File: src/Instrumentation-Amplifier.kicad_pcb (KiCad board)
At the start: 2 copper layers, 24.1 x 34.3 mm, 10 parts, among them J1 PPTC041LFBN-RC, J2 PPTC041LFBN-RC, U1 LM7812_SMD, U2 AD623ARZ-R7

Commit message: Cleaned up file structure
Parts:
- D1: value LTST-C150GKT -> LED_LTST-C150GKT_LTO
- U2: value AD623ARZ-R7 -> R_8_ADI

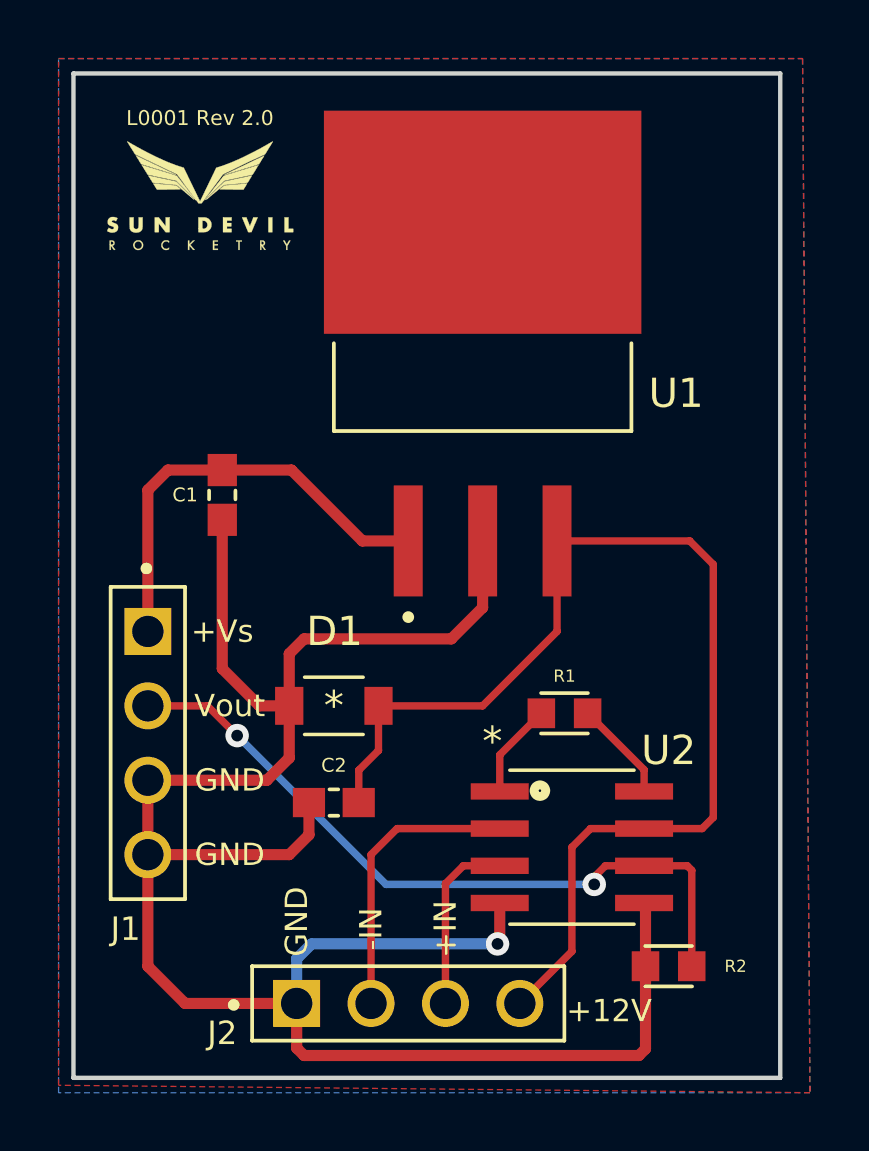
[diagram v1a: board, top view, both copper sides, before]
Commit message: Updated PCB with new connectors
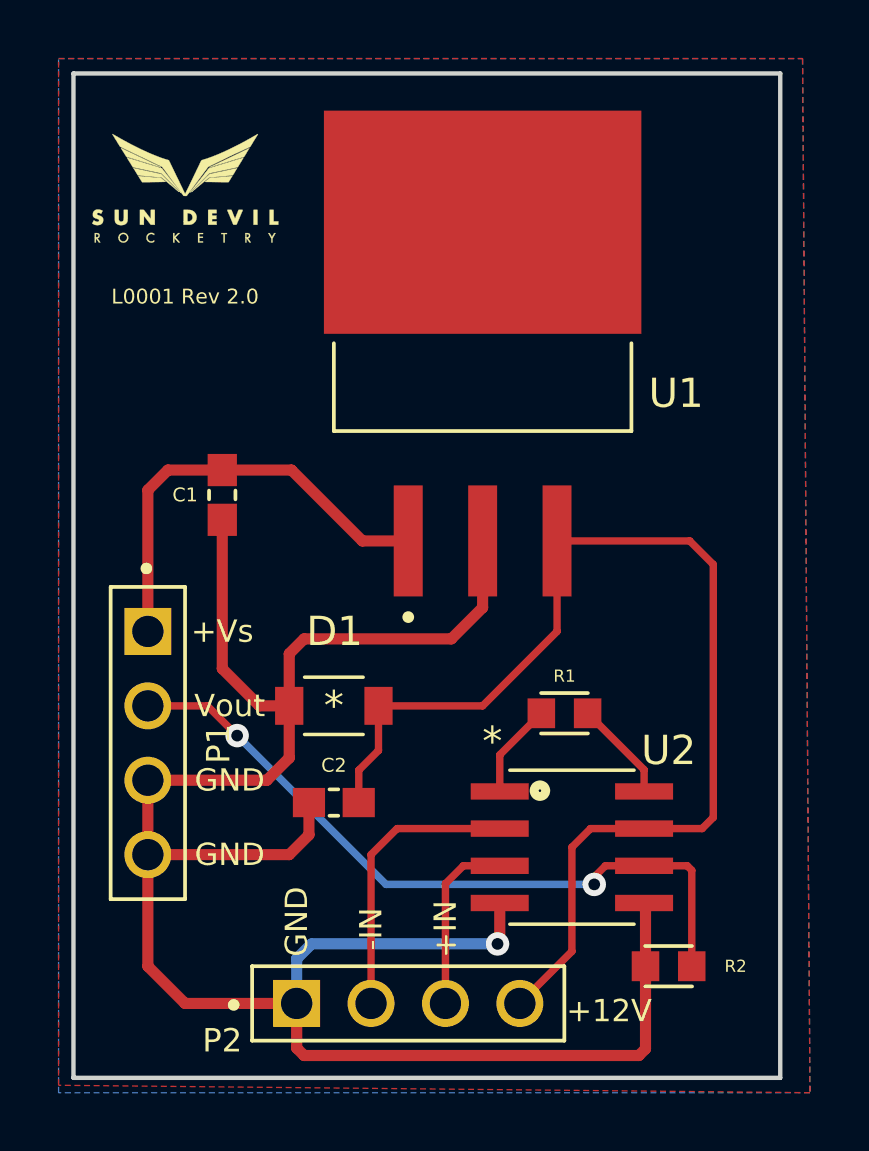
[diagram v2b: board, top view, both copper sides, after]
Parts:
- removed J1, J2: PPTC041LFBN-RC, Instrumentation-Amplifier:PPTC041LFBN-RC
- added P1: 2043-1X04G00DAU, Instrumentation-Amplifier:2043-1X04G00DAU, F.Cu at (106.7, 123.2)
- added P2: 2043-1X04G00DAU, Instrumentation-Amplifier:2043-1X04G00DAU, F.Cu at (115.6, 132.1)
- D1: value LED_LTST-C150GKT_LTO -> LTST-C150GKT
- U2: value R_8_ADI -> AD623ARZ-R7
- moved G*** 0.57 mm to (108.0, 104.1)
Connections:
- net /Vout renamed VOUT
- net ~ renamed +12V

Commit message: Added mounting holes
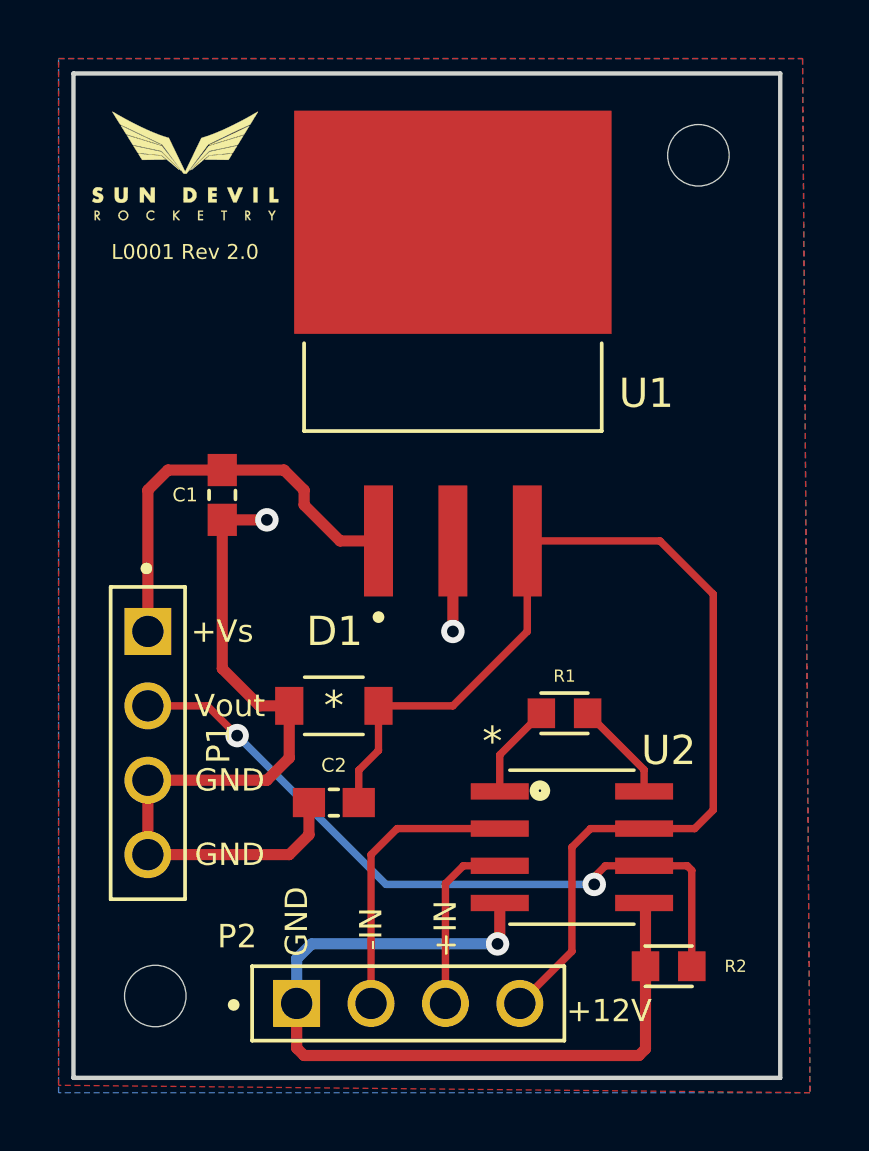
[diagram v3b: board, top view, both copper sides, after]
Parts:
- removed G***: LOGO, Instrumentation-Amplifier:logo2
- added H1: Mounting-Hole, Instrumentation-Amplifier:MountingHole_2.1mm, F.Cu at (106.9, 131.8)
- added H2: Mounting-Hole, Instrumentation-Amplifier:MountingHole_2.1mm, F.Cu at (125.5, 103.1)
- added LOGO1: Logo, Instrumentation-Amplifier:logo2, F.Cu at (108.0, 103.4)
- moved U1 1.02 mm to (117.1, 109.9)
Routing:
- net Earth: track 73.6 -> 57.5 mm, vias 1 -> 3
- net +12V: track 39.4 -> 38.7 mm
- net /+Vs: track 15.0 -> 14.3 mm

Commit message: Added new 3D view image
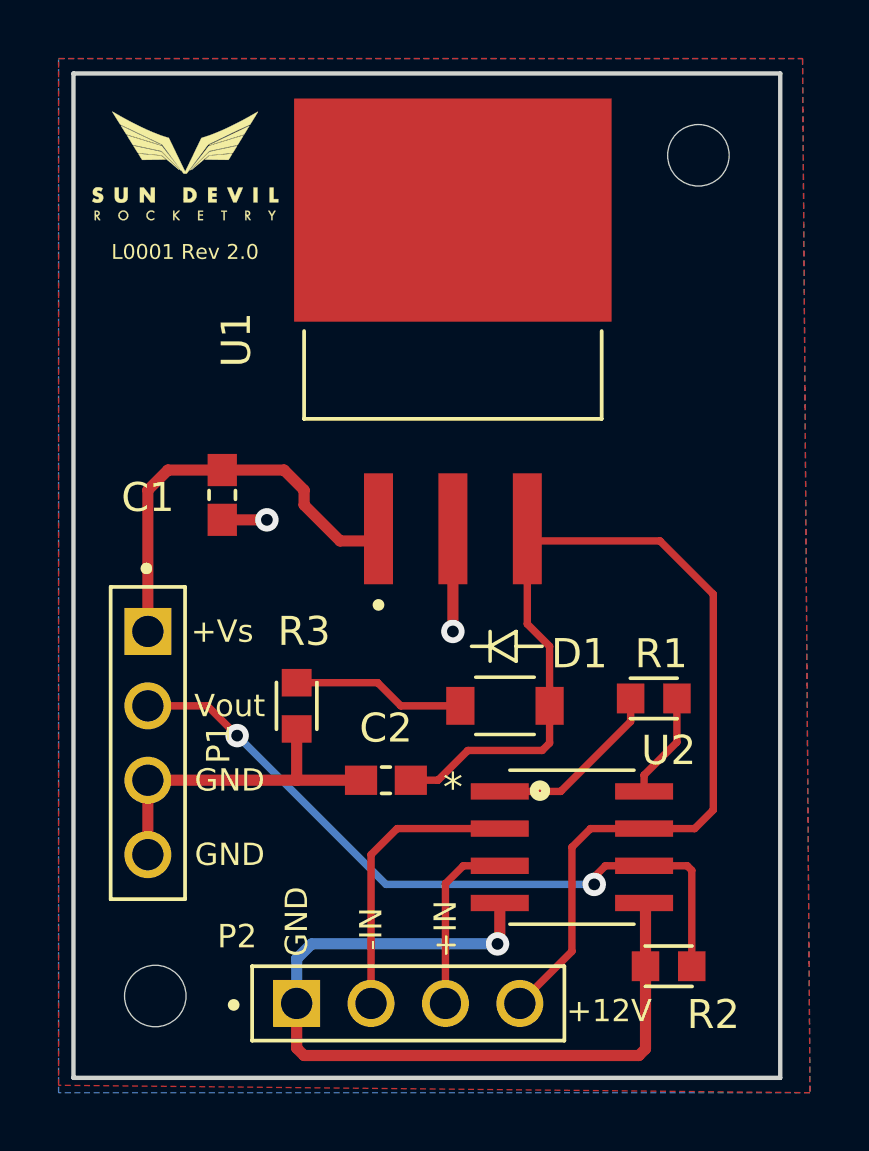
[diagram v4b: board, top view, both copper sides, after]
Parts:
- added R3: 2k, Instrumentation-Amplifier:RES_0603, F.Cu at (111.8, 121.9)
- D1: value LTST-C150GKT -> LED_LTST-C150GKT_LTO
- moved D1 5.84 mm to (118.9, 121.9)
- moved R1 3.09 mm to (124.0, 121.7)
- moved C2 1.93 mm to (114.8, 124.5)
- moved U1 0.42 mm to (117.1, 109.5)
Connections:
- D1 pad 1: Earth -> Net-(D1-Pad1)
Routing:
- net Earth: track 57.5 -> 44.8 mm
- net Net-(D1-Pad1): track 0.00 -> 5.92 mm
- net Net-(R1-Pad1): track 3.26 -> 6.25 mm
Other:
- net class Default removed
- net class Power removed
